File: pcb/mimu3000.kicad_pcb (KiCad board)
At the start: 2 copper layers, 54.8 x 40 mm, 18 parts, among them J1 OPT, SW1 ONOFF, SW2 SW_DPDT_x2, U1 AQY211EH, U2 ATTINY88AU

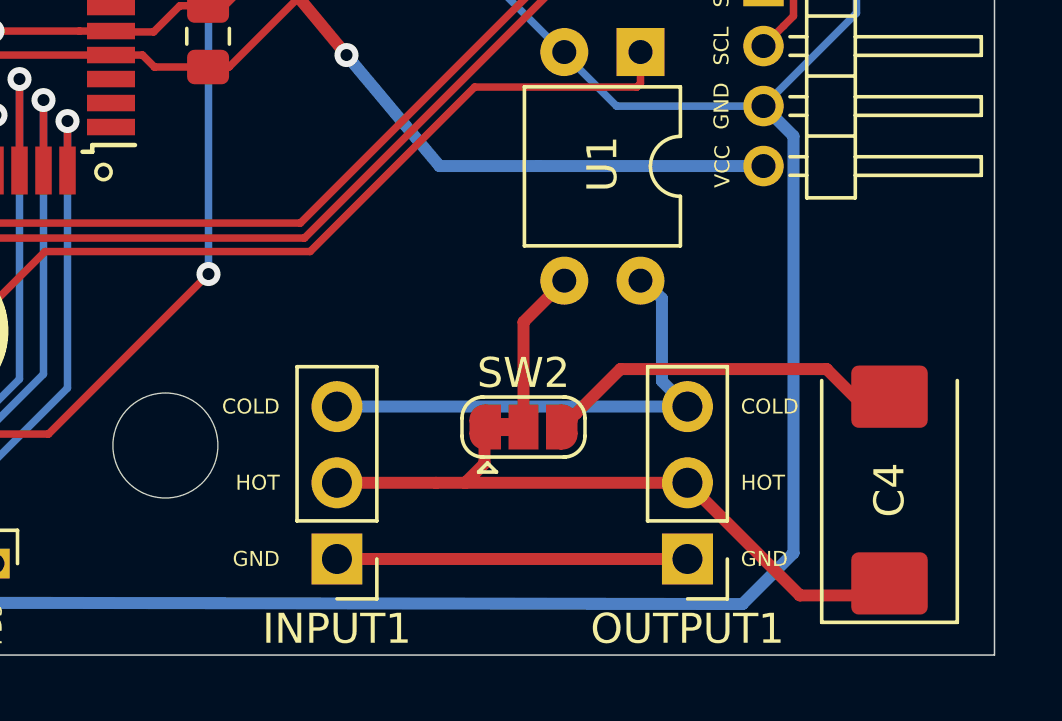
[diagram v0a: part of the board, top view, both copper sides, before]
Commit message: Use electrolyte caps
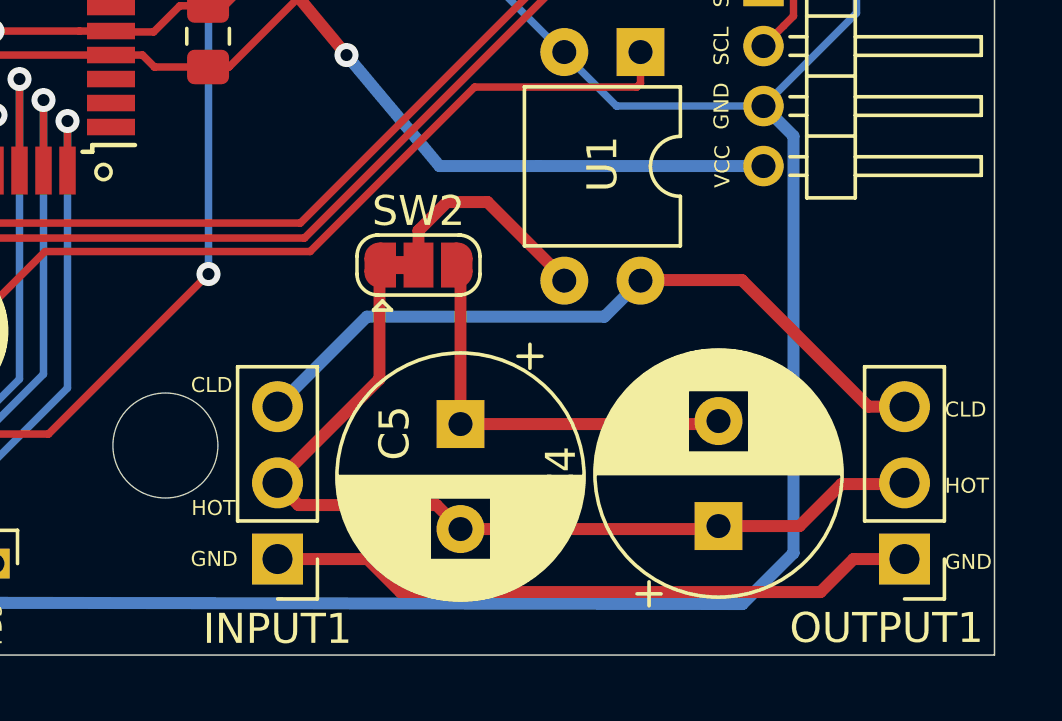
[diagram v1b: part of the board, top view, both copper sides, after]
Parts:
- added C5: 1000uF, Capacitor_THT:CP_Radial_D8.0mm_P3.50mm, F.Cu at (201.2, 119.3)
- C4: footprint Capacitor_Tantalum_SMD:CP_EIA-7343-15_Kemet-W -> Capacitor_THT:CP_Radial_D8.0mm_P3.50mm
- moved OUTPUT1 7.24 mm to (216.0, 123.8)
- moved SW2 6.44 mm to (199.8, 114.0)
- moved C4 5.82 mm to (209.8, 122.7)
- moved INPUT1 1.98 mm to (195.1, 123.8)
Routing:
- net Net-(INPUT1-Pad1): track 11.7 -> 21.8 mm
- net Net-(C4-Pad1): track 22.5 -> 30.5 mm
- net Net-(INPUT1-Pad3): track 16.5 -> 24.4 mm
- net Net-(SW2-Pad2): track 5.48 -> 7.52 mm
- net Net-(C4-Pad2): track 12.8 -> 13.7 mm
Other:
- board text added: "CLD"
- board text removed: "COLD"

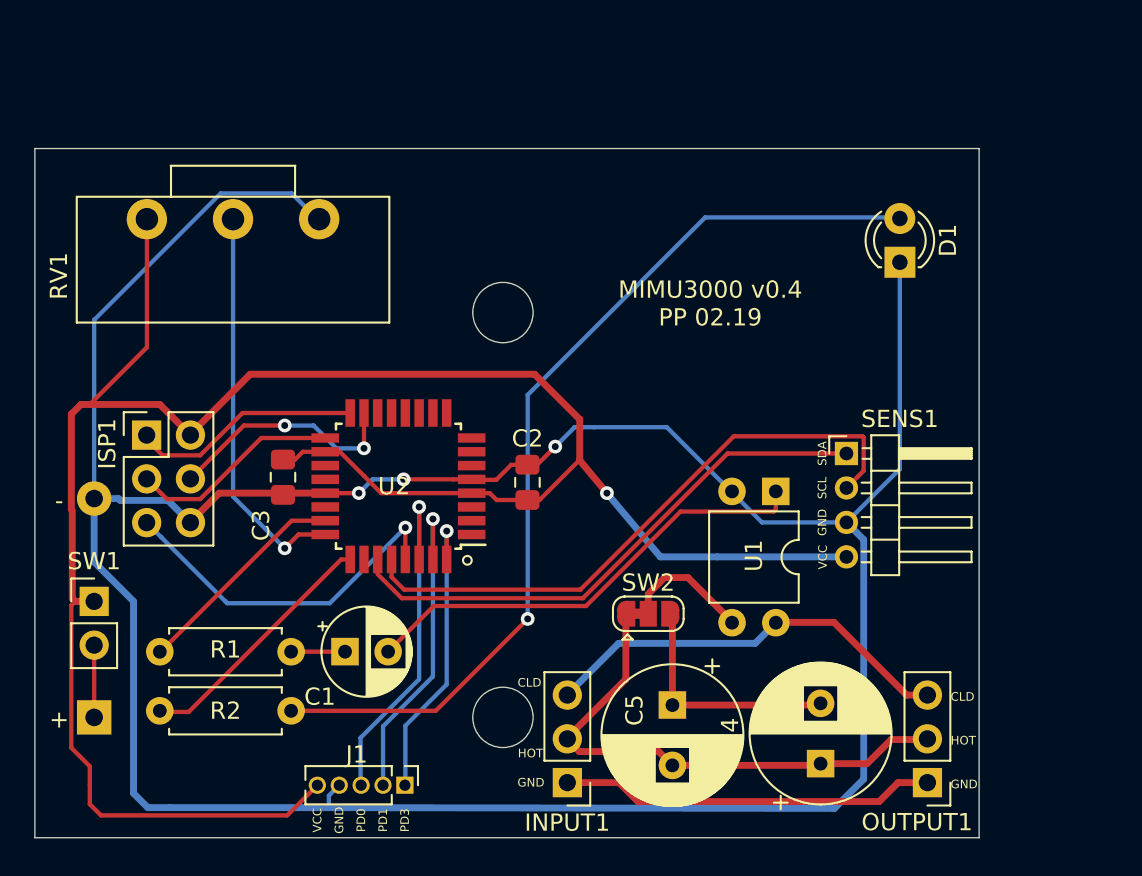
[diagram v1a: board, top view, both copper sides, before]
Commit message: Flipped Sensor to save space
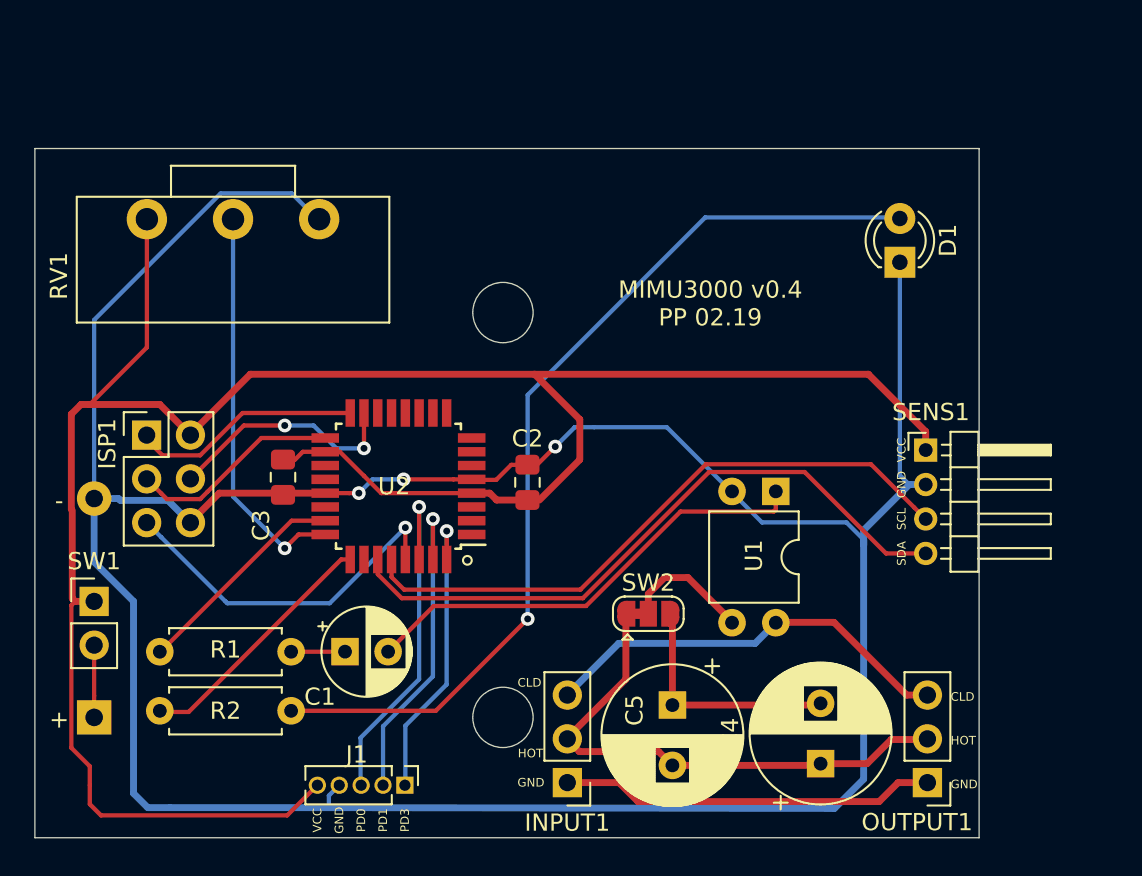
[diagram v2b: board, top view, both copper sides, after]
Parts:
- moved SENS1 4.60 mm to (215.9, 104.5)
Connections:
- SENS1 pad 1: SDA -> +3V0
- SENS1 pad 2: SCL -> GND
- SENS1 pad 3: GND -> SCL
- SENS1 pad 4: +3V0 -> SDA
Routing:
- net +3V0: track 123.7 -> 130.7 mm, vias 1 -> 0
- net SDA: track 32.0 -> 38.1 mm
- net GND: track 171.4 -> 173.7 mm
- net SCL: track 35.8 -> 36.7 mm
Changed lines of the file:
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@@
     (thickness 1.6)
     (drawings 35)
-    (tracks 197)
+    (tracks 199)
     (zones 0)
     (modules 19)
@@
   )
   (setup
-    (last_trace_width 0.4)
+    (last_trace_width 0.25)
     (user_trace_width 0.4)
     (trace_clearance 0.2)
@@
   )
   (module Connector_PinHeader_2.00mm:PinHeader_1x04_P2.00mm_Horizontal (layer F.Cu)
-    (at 211.3 104.7)
+    (at 215.9 104.5)
     (descr "Through hole angled pin header, 1x04, 2.00mm pitch, 4.2mm pin length, single row")
     (tags "Through hole angled pin header THT 1x04 2.00mm single row")
-    (fp_text reference SENS1 (at 3.1 -2) (layer F.SilkS)
-      (effects (font (size 1 1) (thickness 0.15)))
-    )
-    (fp_text value Sens (at 3.1 8) (layer F.Fab)
+    (fp_text reference SENS1 (at 0.3 -2.2) (layer F.SilkS)
+      (effects (font (size 1 1) (thickness 0.15)))
+    )
+    (fp_text value Sens (at 0.4 8.1) (layer F.Fab)
       (effects (font (size 1 1) (thickness 0.15)))
     )
@@
     (fp_line (start 1.875 -1) (end 3 -1) (layer F.Fab) (width 0.1))
     (pad 4 thru_hole oval (at 0 6) (size 1.35 1.35) (drill 0.8) (layers *.Cu *.Mask)
+      (net 20 SDA))
+    (pad 3 thru_hole oval (at 0 4) (size 1.35 1.35) (drill 0.8) (layers *.Cu *.Mask)
+      (net 19 SCL))
+    (pad 2 thru_hole oval (at 0 2) (size 1.35 1.35) (drill 0.8) (layers *.Cu *.Mask)
+      (net 11 GND))
+    (pad 1 thru_hole rect (at 0 0) (size 1.35 1.35) (drill 0.8) (layers *.Cu *.Mask)
       (net 12 +3V0))
-    (pad 3 thru_hole oval (at 0 4) (size 1.35 1.35) (drill 0.8) (layers *.Cu *.Mask)
-      (net 11 GND))
-    (pad 2 thru_hole oval (at 0 2) (size 1.35 1.35) (drill 0.8) (layers *.Cu *.Mask)
-      (net 19 SCL))
-    (pad 1 thru_hole rect (at 0 0) (size 1.35 1.35) (drill 0.8) (layers *.Cu *.Mask)
-      (net 20 SDA))
     (model ${KISYS3DMOD}/Connector_PinHeader_2.00mm.3dshapes/PinHeader_1x04_P2.00mm_Horizontal.wrl
       (offset (xyz 0 0 2))
@@
     (effects (font (size 0.5 0.5) (thickness 0.1)) (justify left))
   )
-  (gr_text SDA (at 209.9 104.7 90) (layer F.SilkS)
+  (gr_text SDA (at 214.5 110.5 90) (layer F.SilkS)
     (effects (font (size 0.5 0.5) (thickness 0.1)))
   )
-  (gr_text SCL (at 209.9 106.7 90) (layer F.SilkS)
+  (gr_text SCL (at 214.5 108.5 90) (layer F.SilkS)
     (effects (font (size 0.5 0.5) (thickness 0.1)))
   )
-  (gr_text GND (at 209.9 108.7 90) (layer F.SilkS)
+  (gr_text GND (at 214.5 106.5 90) (layer F.SilkS)
     (effects (font (size 0.5 0.5) (thickness 0.1)))
   )
-  (gr_text VCC (at 209.93 110.714 90) (layer F.SilkS)
+  (gr_text VCC (at 214.5 104.5 90) (layer F.SilkS)
     (effects (font (size 0.5 0.5) (thickness 0.1)))
   )
@@
   (segment (start 200.874999 103.174999) (end 206.4 108.7) (width 0.25) (layer B.Cu) (net 11))
   (segment (start 196.651999 103.174999) (end 200.874999 103.174999) (width 0.25) (layer B.Cu) (net 11))
-  (segment (start 212.300001 109.700001) (end 212.300001 123.599999) (width 0.4) (layer B.Cu) (net 11))
-  (segment (start 211.3 108.7) (end 212.300001 109.700001) (width 0.4) (layer B.Cu) (net 11))
+  (segment (start 211.3 108.7) (end 212.300001 109.700001) (width 0.25) (layer B.Cu) (net 11))
   (segment (start 212.300001 123.599999) (end 210.6 125.3) (width 0.4) (layer B.Cu) (net 11))
   (segment (start 210.6 125.3) (end 181.135992 125.25201) (width 0.4) (layer B.Cu) (net 11))
-  (segment (start 211.3 108.7) (end 214.4 105.6) (width 0.25) (layer B.Cu) (net 11))
-  (segment (start 214.4 105.6) (end 214.4 93.7) (width 0.25) (layer B.Cu) (net 11))
   (via (at 185.6 106.2) (size 0.8) (drill 0.4) (layers F.Cu B.Cu) (net 11))
   (segment (start 188.5 106.2) (end 185.6 106.2) (width 0.25) (layer F.Cu) (net 11))
@@
   (segment (start 169.054213 107.315) (end 169.161214 107.422001) (width 0.4) (layer B.Cu) (net 11))
   (segment (start 171.922001 107.422001) (end 173.2 108.7) (width 0.4) (layer B.Cu) (net 11))
+  (segment (start 212.3 109.145406) (end 212.3 110) (width 0.4) (layer B.Cu) (net 11))
+  (segment (start 215.9 106.5) (end 214.945406 106.5) (width 0.4) (layer B.Cu) (net 11))
+  (segment (start 212.300001 109.700001) (end 212.3 110) (width 0.4) (layer B.Cu) (net 11))
+  (segment (start 214.945406 106.5) (end 212.3 109.145406) (width 0.4) (layer B.Cu) (net 11))
+  (segment (start 212.3 110) (end 212.300001 123.599999) (width 0.4) (layer B.Cu) (net 11))
+  (segment (start 214.4 105.954594) (end 214.945406 106.5) (width 0.25) (layer B.Cu) (net 11))
+  (segment (start 214.4 93.7) (end 214.4 105.954594) (width 0.25) (layer B.Cu) (net 11))
   (segment (start 167.386 122.852) (end 167.386 123.952) (width 0.25) (layer F.Cu) (net 12))
   (segment (start 166.314999 113.509001) (end 166.314999 121.780999) (width 0.25) (layer F.Cu) (net 12))
@@
   (segment (start 178.6 105.05) (end 179.3 105.05) (width 0.25) (layer F.Cu) (net 12))
   (segment (start 179.75 104.6) (end 181 104.6) (width 0.25) (layer F.Cu) (net 12))
-  (segment (start 190.6 107) (end 191 107.4) (width 0.25) (layer F.Cu) (net 12))
-  (segment (start 189.55 107) (end 190.6 107) (width 0.25) (layer F.Cu) (net 12))
+  (segment (start 190.6 107) (end 191 107.4) (width 0.4) (layer F.Cu) (net 12))
+  (segment (start 189.55 107) (end 190.6 107) (width 0.4) (layer F.Cu) (net 12))
   (segment (start 191.001 107.399) (end 191 107.4) (width 0.25) (layer F.Cu) (net 12))
-  (segment (start 192.786 107.399) (end 191.001 107.399) (width 0.25) (layer F.Cu) (net 12))
+  (segment (start 192.786 107.399) (end 191.001 107.399) (width 0.4) (layer F.Cu) (net 12))
   (segment (start 183.3 106) (end 184.3 107) (width 0.25) (layer F.Cu) (net 12))
   (segment (start 184.3 107) (end 189.6 107) (width 0.25) (layer F.Cu) (net 12))
@@
   (segment (start 195.8 105.073002) (end 195.825001 105.048001) (width 0.25) (layer F.Cu) (net 12))
   (segment (start 195.8 105.085) (end 195.8 105.073002) (width 0.25) (layer F.Cu) (net 12))
-  (segment (start 193.486 107.399) (end 195.8 105.085) (width 0.25) (layer F.Cu) (net 12))
+  (segment (start 193.486 107.399) (end 195.8 105.085) (width 0.4) (layer F.Cu) (net 12))
   (segment (start 192.786 107.399) (end 193.486 107.399) (width 0.25) (layer F.Cu) (net 12))
-  (segment (start 197.4 107) (end 195.8 105.073002) (width 0.4) (layer F.Cu) (net 12))
-  (via (at 197.4 107) (size 0.8) (drill 0.4) (layers F.Cu B.Cu) (net 12))
-  (segment (start 203.8 110.7) (end 211.3 110.7) (width 0.4) (layer B.Cu) (net 12))
-  (segment (start 197.4 107) (end 200.5 110.7) (width 0.4) (layer B.Cu) (net 12))
-  (segment (start 200.5 110.7) (end 203.8 110.7) (width 0.4) (layer B.Cu) (net 12))
+  (segment (start 212.575 100.1) (end 215.9 103.425) (width 0.4) (layer F.Cu) (net 12))
+  (segment (start 193.2 100.1) (end 212.575 100.1) (width 0.4) (layer F.Cu) (net 12))
+  (segment (start 215.9 103.425) (end 215.9 104.5) (width 0.4) (layer F.Cu) (net 12))
   (segment (start 181.05 108.6) (end 179.1 108.6) (width 0.25) (layer F.Cu) (net 13))
   (segment (start 179.1 108.6) (end 171.5 116.2) (width 0.25) (layer F.Cu) (net 13))
@@
   (segment (start 185.7 120.5) (end 185.7 124) (width 0.25) (layer B.Cu) (net 18))
   (segment (start 184.9 110.85) (end 184.9 111.873592) (width 0.25) (layer F.Cu) (net 19))
-  (segment (start 212.300001 105.699999) (end 211.974999 106.025001) (width 0.25) (layer F.Cu) (net 19))
   (segment (start 184.9 111.873592) (end 185.626408 112.6) (width 0.25) (layer F.Cu) (net 19))
-  (segment (start 195.86359 112.6) (end 204.763591 103.699999) (width 0.25) (layer F.Cu) (net 19))
-  (segment (start 204.763591 103.699999) (end 212.235001 103.699999) (width 0.25) (layer F.Cu) (net 19))
-  (segment (start 212.300001 103.764999) (end 212.300001 105.699999) (width 0.25) (layer F.Cu) (net 19))
-  (segment (start 212.235001 103.699999) (end 212.300001 103.764999) (width 0.25) (layer F.Cu) (net 19))
-  (segment (start 211.974999 106.025001) (end 211.3 106.7) (width 0.25) (layer F.Cu) (net 19))
   (segment (start 185.626408 112.6) (end 195.86359 112.6) (width 0.25) (layer F.Cu) (net 19))
-  (segment (start 211.3 104.7) (end 204.4 104.7) (width 0.25) (layer F.Cu) (net 20))
-  (segment (start 204.4 104.7) (end 196 113.1) (width 0.25) (layer F.Cu) (net 20))
+  (segment (start 212.724989 105.324989) (end 215.225001 107.825001) (width 0.25) (layer F.Cu) (net 19))
+  (segment (start 195.86359 112.6) (end 203.138601 105.324989) (width 0.25) (layer F.Cu) (net 19))
+  (segment (start 203.138601 105.324989) (end 212.724989 105.324989) (width 0.25) (layer F.Cu) (net 19))
+  (segment (start 215.225001 107.825001) (end 215.9 108.5) (width 0.25) (layer F.Cu) (net 19))
   (segment (start 185.489998 113.1) (end 184.1 111.710002) (width 0.25) (layer F.Cu) (net 20))
   (segment (start 196 113.1) (end 185.489998 113.1) (width 0.25) (layer F.Cu) (net 20))
   (segment (start 184.1 111.710002) (end 184.1 111) (width 0.25) (layer F.Cu) (net 20))
+  (segment (start 203.325001 105.774999) (end 208.874999 105.774999) (width 0.25) (layer F.Cu) (net 20))
+  (segment (start 196 113.1) (end 203.325001 105.774999) (width 0.25) (layer F.Cu) (net 20))
+  (segment (start 208.874999 105.774999) (end 213.6 110.5) (width 0.25) (layer F.Cu) (net 20))
+  (segment (start 213.6 110.5) (end 215.9 110.5) (width 0.25) (layer F.Cu) (net 20))
   (segment (start 201.2 119.3) (end 209.7 119.3) (width 0.4) (layer F.Cu) (net 21))
   (segment (start 201.2 119.3) (end 201.2 114.2) (width 0.4) (layer F.Cu) (net 21))

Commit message: Fixed wrong-sized pitch of sensor, corrected witdh of a track. easier footprint for opto
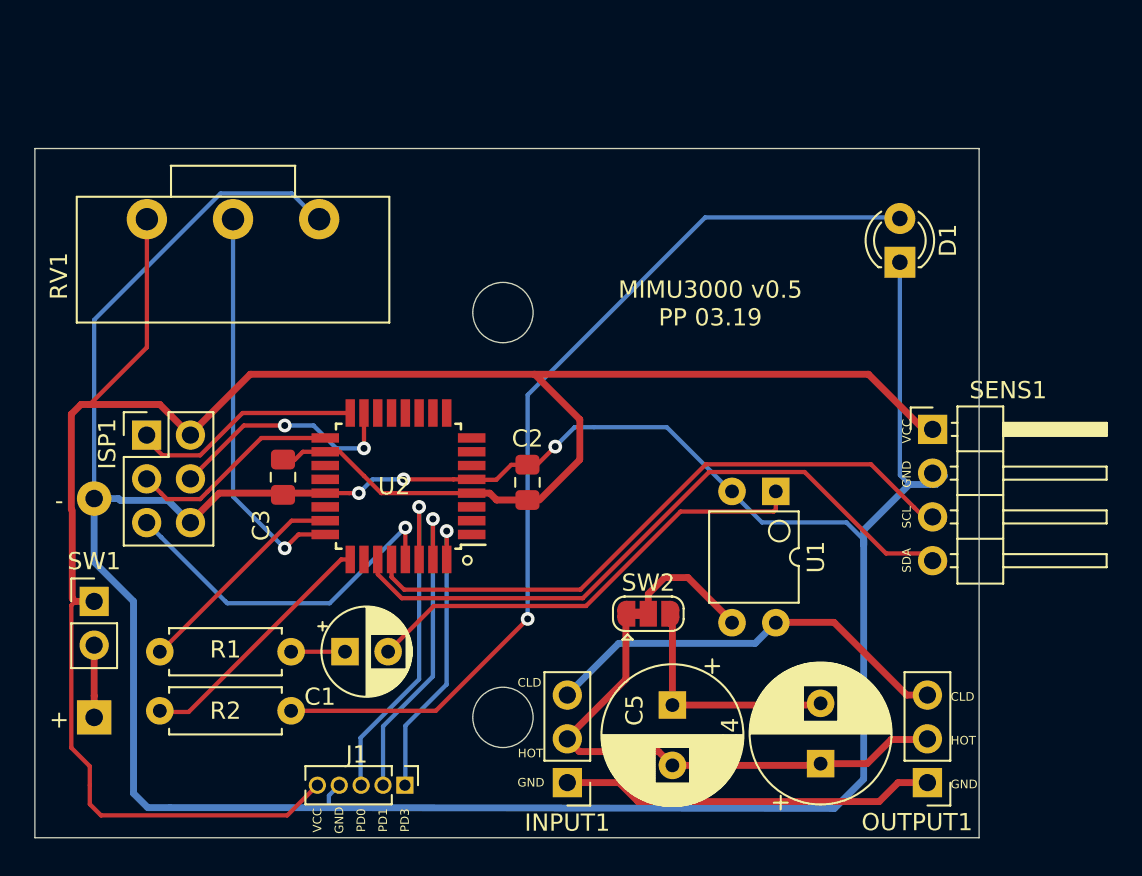
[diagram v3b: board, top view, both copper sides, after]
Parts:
- SENS1: footprint Connector_PinHeader_2.00mm:PinHeader_1x04_P2.00mm_Horizontal -> Connector_PinHeader_2.54mm:PinHeader_1x04_P2.54mm_Horizontal
- U1: footprint Package_DIP:DIP-4_W7.62mm -> custom:DIP-4_bubble_W7.62mm
- moved SENS1 1.26 mm to (216.3, 103.3)
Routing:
- net SDA: track 38.1 -> 39.7 mm
- net GND: track 173.7 -> 175.0 mm
- net SCL: track 36.7 -> 37.8 mm
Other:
- board text added: "MIMU3000 v0.5 PP 03.19"
- board text removed: "MIMU3000 v0.4 PP 02.19"
